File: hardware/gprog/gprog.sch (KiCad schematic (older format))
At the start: 20 parts, among them P1 ISP x2560, P2 USB, P3 ISP x48, U1 74HC126, X1 12MHz

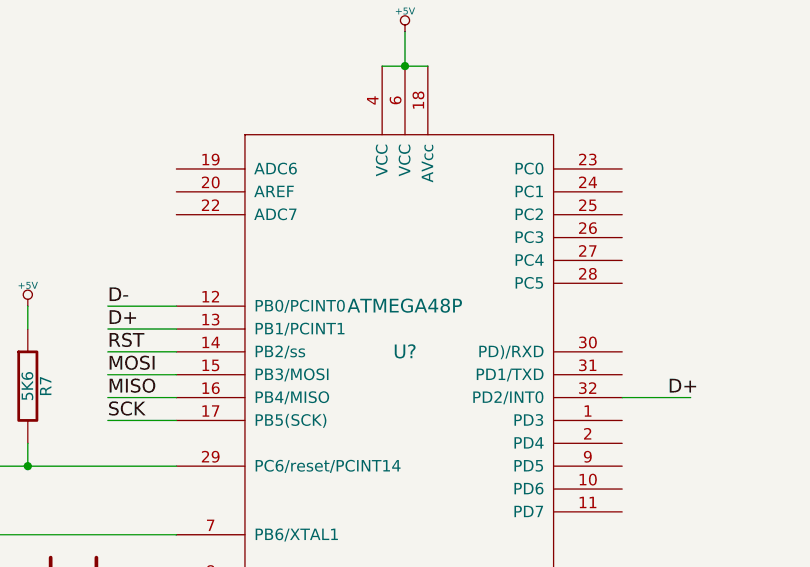
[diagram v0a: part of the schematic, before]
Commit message: Minor correction to GPRO v1.0 Schematic and component library.
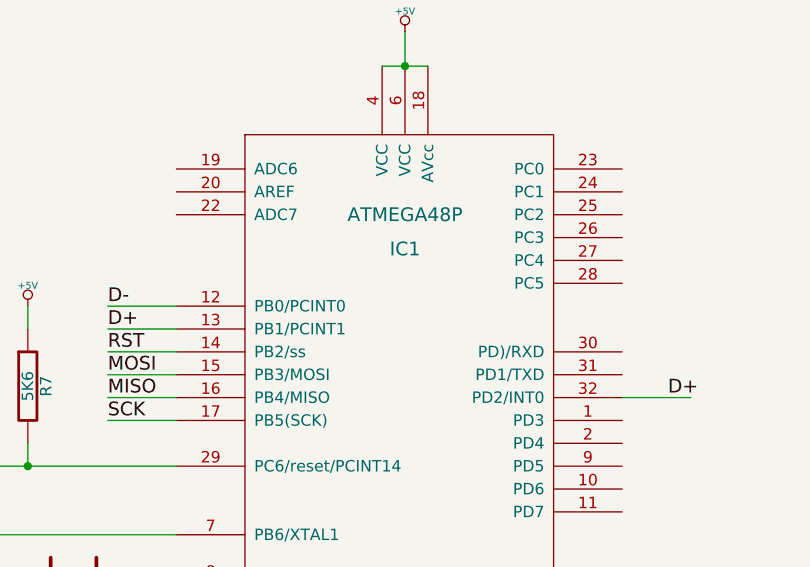
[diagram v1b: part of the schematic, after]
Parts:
- gave numbers to parts that had none: 1
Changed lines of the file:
@@
-EESchema Schematic File Version 2  date 23/11/2011 2:39:53 p.m.
+EESchema Schematic File Version 2  date 23/11/2011 3:01:04 p.m.
 LIBS:power
 LIBS:device
@@
 $EndComp
 $Comp
-L ATMEGA48P U?
+L ATMEGA48P IC1
 U 1 1 4ECC4939
 P 4200 5350
-F 0 "U?" H 4200 5350 60  0000 C CNN
-F 1 "ATMEGA48P" H 4200 5550 60  0000 C CNN
+F 0 "IC1" H 4200 5800 60  0000 C CNN
+F 1 "ATMEGA48P" H 4200 5950 60  0000 C CNN
 	1    4200 5350
 	1    0    0    -1

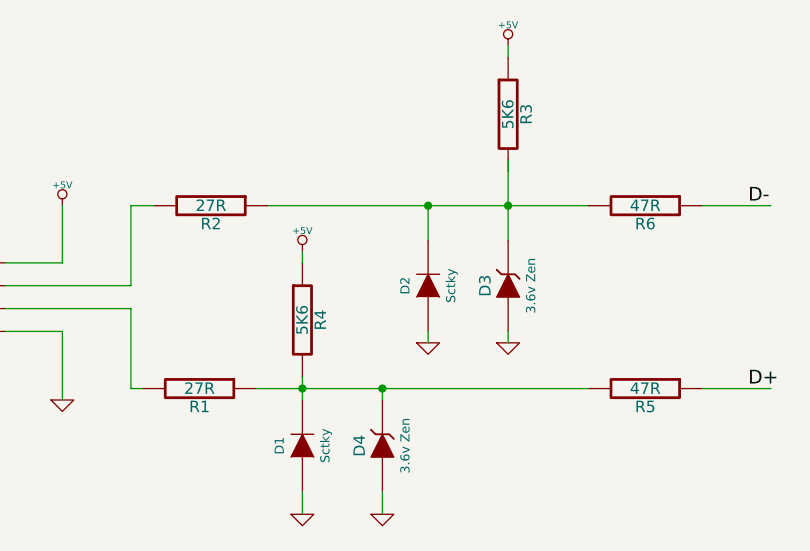
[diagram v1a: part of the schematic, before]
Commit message: As advised by JWB, corrected GPROG (USBasp) programmer circuit.
Only pull-up D- to tell USB host we are a slow speed device. Changed resistor
to 3K6 from 5K6 for better voltage matching, in theory.
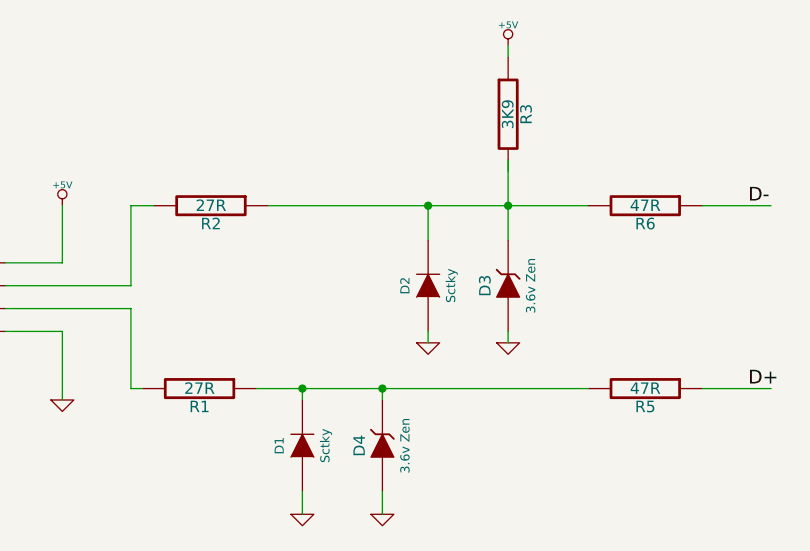
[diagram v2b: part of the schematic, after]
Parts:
- removed R4: 5K6, symbol R
- R3: value 5K6 -> 3K9
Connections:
- wire segments 93 -> 91
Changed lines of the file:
@@
-EESchema Schematic File Version 2  date 23/11/2011 3:01:04 p.m.
+EESchema Schematic File Version 2  date 24/11/2011 2:36:36 p.m.
 LIBS:power
 LIBS:device
@@
 Sheet 1 1
 Title "G9X USB Programmer"
-Date "23 nov 2011"
+Date "24 nov 2011"
 Rev "1.0"
 Comp ""
@@
 Wire Wire Line
 	4150 2400 4150 2350
-Wire Wire Line
-	3250 2050 3250 2000
 Connection ~ 3800 1800
 Wire Wire Line
@@
 Wire Wire Line
 	3250 2600 3050 2600
-Wire Wire Line
-	3250 2550 3250 2600
 Wire Wire Line
 	3250 2600 3250 2650
@@
 $EndComp
 $Comp
-L +5V #PWR?
-U 1 1 4E9129FB
-P 3250 2000
-F 0 "#PWR?" H 3250 2090 20  0001 C CNN
-F 1 "+5V" H 3250 2090 30  0000 C CNN
-	1    3250 2000
-	1    0    0    -1
-$EndComp
-$Comp
-L R R4
-U 1 1 4E9129C4
-P 3250 2300
-F 0 "R4" V 3330 2300 50  0000 C CNN
-F 1 "5K6" V 3250 2300 50  0000 C CNN
-	1    3250 2300
-	1    0    0    -1
-$EndComp
-$Comp
 L R R5
 U 1 1 4E912987
@@
 P 4150 1400
 F 0 "R3" V 4230 1400 50  0000 C CNN
-F 1 "5K6" V 4150 1400 50  0000 C CNN
+F 1 "3K9" V 4150 1400 50  0000 C CNN
 	1    4150 1400
 	1    0    0    -1

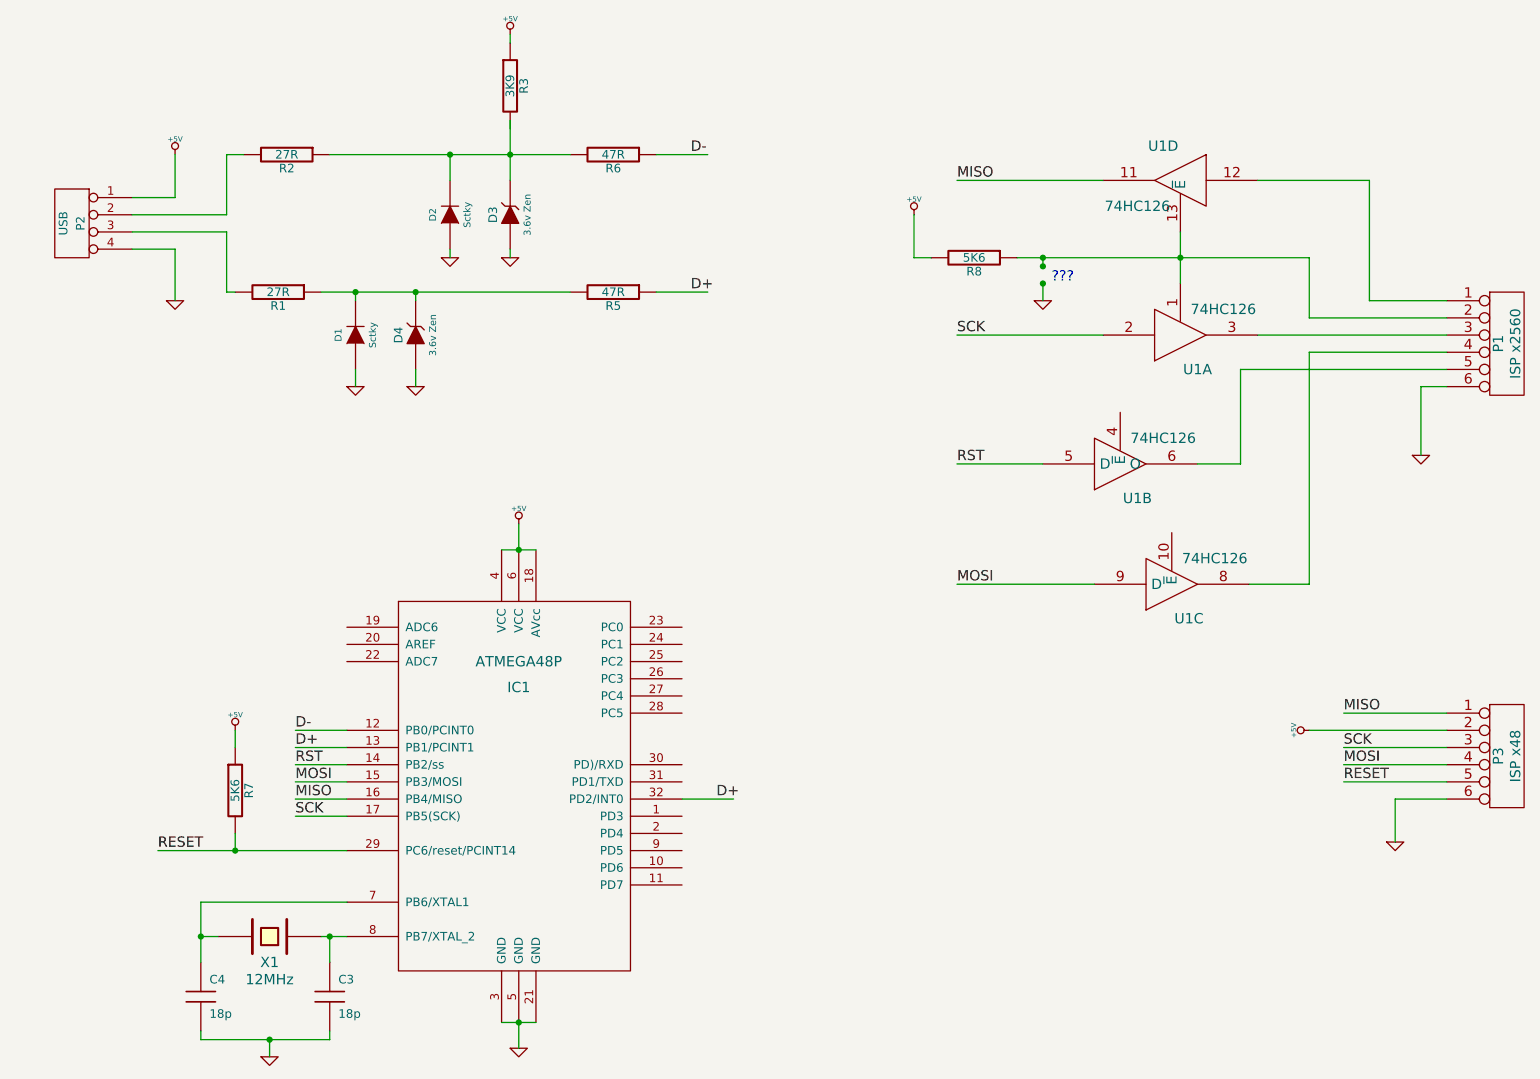
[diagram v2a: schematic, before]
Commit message: Completed draft 1 of gprog KiCAD version PCB.
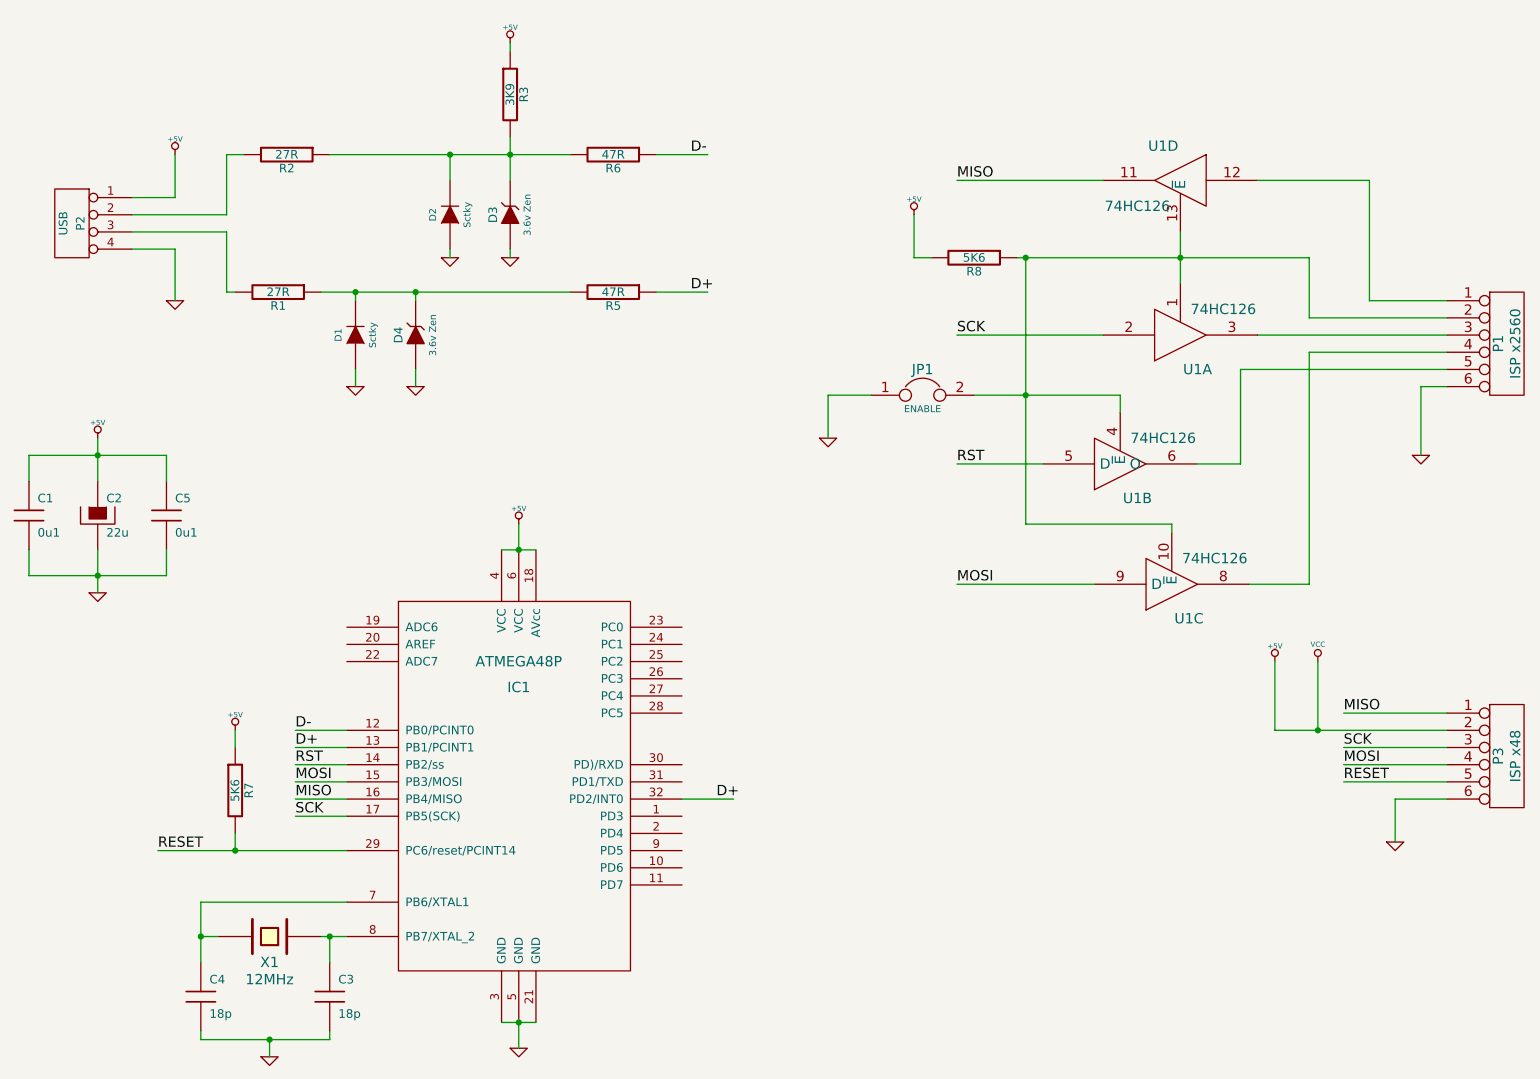
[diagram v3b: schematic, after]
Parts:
- added C1, C5: 0u1, symbol C
- added C2: 22u, symbol CAPAPOL
- added JP1: ENABLE, symbol JUMPER
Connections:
- net labels added: VCC
- wire segments 91 -> 92
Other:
- note removed: "???"
- moved on the sheet: R3
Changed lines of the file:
@@
-EESchema Schematic File Version 2  date 24/11/2011 2:36:36 p.m.
+EESchema Schematic File Version 2  date 27/11/2011 12:33:56 a.m.
 LIBS:power
 LIBS:device
@@
 Sheet 1 1
 Title "G9X USB Programmer"
-Date "24 nov 2011"
+Date "26 nov 2011"
 Rev "1.0"
 Comp ""
@@
 Comment4 ""
 $EndDescr
-Text Notes 7300 2550 0    60   ~ 0
-???
-Connection ~ 7250 2550
-Wire Wire Line
-	7250 2650 7250 2550
-Wire Wire Line
-	7100 2400 7250 2400
-Wire Wire Line
-	7250 2400 8050 2400
-Wire Wire Line
-	8050 2400 8800 2400
+Wire Wire Line
+	8600 5150 8600 4750
+Wire Wire Line
+	6850 3200 7700 3200
+Connection ~ 7150 3200
+Wire Wire Line
+	7700 3200 7700 3300
+Wire Wire Line
+	1750 3450 1750 3700
+Wire Wire Line
+	2150 3550 2150 3700
+Wire Wire Line
+	2150 3550 1350 3550
+Wire Wire Line
+	1350 3550 1350 3700
+Connection ~ 1750 4250
+Wire Wire Line
+	7100 2400 8800 2400
 Wire Wire Line
 	6600 2400 6500 2400
@@
 	6500 2400 6500 2150
 Wire Wire Line
-	2350 6900 2350 6950
-Wire Wire Line
-	2350 6950 2750 6950
-Wire Wire Line
-	2750 6950 3100 6950
+	2350 6950 2350 6900
+Wire Wire Line
+	2350 6950 3100 6950
 Wire Wire Line
 	3100 6950 3100 6900
 Connection ~ 2350 6350
 Wire Wire Line
-	2350 6500 2350 6350
-Wire Wire Line
-	2350 6350 2350 6150
+	2350 6500 2350 6150
 Wire Wire Line
 	2350 6150 3200 6150
@@
 	2550 5150 2550 5250
 Wire Wire Line
-	3200 5850 2550 5850
-Wire Wire Line
-	2550 5850 2100 5850
+	2100 5850 3200 5850
 Wire Wire Line
 	3200 5250 2900 5250
@@
 Connection ~ 4200 4100
 Wire Wire Line
-	4100 4100 4200 4100
-Wire Wire Line
-	4200 4100 4300 4100
+	4300 4100 4100 4100
 Wire Wire Line
 	9300 5800 9300 5550
@@
 	8800 4300 8450 4300
 Wire Wire Line
-	8050 2550 8050 2400
-Wire Wire Line
-	8050 2400 8050 2250
+	8050 2250 8050 2550
 Wire Wire Line
 	8800 2400 8800 2750
@@
 	2600 1800 2500 1800
 Wire Wire Line
-	3100 1800 3800 1800
-Wire Wire Line
-	3800 1800 4150 1800
-Wire Wire Line
-	4150 1800 4500 1800
-Wire Wire Line
-	4150 1100 4150 1150
+	4500 1800 3100 1800
+Wire Wire Line
+	4150 1200 4150 1150
 Wire Wire Line
 	5000 2600 5300 2600
@@
 	3800 2350 3800 2400
 Wire Wire Line
-	4500 2600 3600 2600
-Wire Wire Line
-	3600 2600 3250 2600
-Wire Wire Line
-	3250 2600 3050 2600
+	3050 2600 4500 2600
 Wire Wire Line
 	3250 2600 3250 2650
@@
 	5000 1800 5300 1800
 Wire Wire Line
-	4150 1600 4150 1800
-Wire Wire Line
-	4150 1800 4150 1950
+	4150 1950 4150 1700
 Wire Wire Line
 	2550 2600 2500 2600
@@
 	7600 1950 6750 1950
 Wire Wire Line
-	9600 5150 8800 5150
+	9600 5150 8600 5150
 Wire Wire Line
 	9600 5350 9000 5350
@@
 	4200 3950 4200 4100
 Wire Wire Line
-	4100 6850 4200 6850
-Wire Wire Line
-	4200 6850 4300 6850
+	4300 6850 4100 6850
 Connection ~ 4200 6850
 Wire Wire Line
@@
 Connection ~ 2550 5850
 Wire Wire Line
-	3050 6350 3100 6350
-Wire Wire Line
-	3100 6350 3200 6350
-Wire Wire Line
-	2350 6350 2450 6350
+	3200 6350 3050 6350
+Wire Wire Line
+	2450 6350 2350 6350
 Wire Wire Line
 	3100 6500 3100 6350
@@
 Connection ~ 2750 6950
 Wire Wire Line
-	7250 2400 7250 2450
-Connection ~ 7250 2400
-Connection ~ 7250 2450
-$Comp
-L GND #PWR?
-U 1 1 4ECC4DFB
-P 7250 2650
-F 0 "#PWR?" H 7250 2650 30  0001 C CNN
-F 1 "GND" H 7250 2580 30  0001 C CNN
-	1    7250 2650
+	2150 4250 2150 4100
+Wire Wire Line
+	2150 4250 1350 4250
+Wire Wire Line
+	1350 4250 1350 4100
+Wire Wire Line
+	1750 4350 1750 4100
+Connection ~ 1750 3550
+Wire Wire Line
+	8000 4000 8000 3950
+Wire Wire Line
+	7150 3950 8000 3950
+Wire Wire Line
+	7150 2400 7150 3950
+Connection ~ 7150 2400
+Wire Wire Line
+	6000 3450 6000 3200
+Wire Wire Line
+	6000 3200 6250 3200
+Wire Wire Line
+	8850 4750 8850 5150
+Connection ~ 8850 5150
+$Comp
+L VCC #PWR01
+U 1 1 4ED0B44E
+P 8850 4750
+F 0 "#PWR01" H 8850 4850 30  0001 C CNN
+F 1 "VCC" H 8850 4850 30  0000 C CNN
+	1    8850 4750
+	1    0    0    -1
+$EndComp
+$Comp
+L GND #PWR02
+U 1 1 4ED0AC2D
+P 6000 3450
+F 0 "#PWR02" H 6000 3450 30  0001 C CNN
+F 1 "GND" H 6000 3380 30  0001 C CNN
+	1    6000 3450
+	1    0    0    -1
+$EndComp
+$Comp
+L JUMPER JP1
+U 1 1 4ED0AC1E
+P 6550 3200
+F 0 "JP1" H 6550 3350 60  0000 C CNN
+F 1 "ENABLE" H 6550 3120 40  0000 C CNN
+	1    6550 3200
+	1    0    0    -1
+$EndComp
+$Comp
+L +5V #PWR03
+U 1 1 4ED08824
+P 1750 3450
+F 0 "#PWR03" H 1750 3540 20  0001 C CNN
+F 1 "+5V" H 1750 3540 30  0000 C CNN
+	1    1750 3450
+	1    0    0    -1
+$EndComp
+$Comp
+L GND #PWR04
+U 1 1 4ED08810
+P 1750 4350
+F 0 "#PWR04" H 1750 4350 30  0001 C CNN
+F 1 "GND" H 1750 4280 30  0001 C CNN
+	1    1750 4350
+	1    0    0    -1
+$EndComp
+$Comp
+L CAPAPOL C2
+U 1 1 4ED087CB
+P 1750 3900
+F 0 "C2" H 1800 4000 50  0000 L CNN
+F 1 "22u" H 1800 3800 50  0000 L CNN
+	1    1750 3900
+	1    0    0    -1
+$EndComp
+$Comp
+L C C5
+U 1 1 4ED087AC
+P 2150 3900
+F 0 "C5" H 2200 4000 50  0000 L CNN
+F 1 "0u1" H 2200 3800 50  0000 L CNN
+	1    2150 3900
+	1    0    0    -1
+$EndComp
+$Comp
+L C C1
+U 1 1 4ED087A6
+P 1350 3900
+F 0 "C1" H 1400 4000 50  0000 L CNN
+F 1 "0u1" H 1400 3800 50  0000 L CNN
+	1    1350 3900
 	1    0    0    -1
 $EndComp
@@
 D+
 $Comp
-L GND #PWR?
+L GND #PWR05
 U 1 1 4ECC4B90
 P 2750 7050
-F 0 "#PWR?" H 2750 7050 30  0001 C CNN
+F 0 "#PWR05" H 2750 7050 30  0001 C CNN
 F 1 "GND" H 2750 6980 30  0001 C CNN
 	1    2750 7050
@@
 $EndComp
 $Comp
-L +5V #PWR?
+L +5V #PWR06
 U 1 1 4ECC4A1D
 P 2550 5150
-F 0 "#PWR?" H 2550 5240 20  0001 C CNN
+F 0 "#PWR06" H 2550 5240 20  0001 C CNN
 F 1 "+5V" H 2550 5240 30  0000 C CNN
 	1    2550 5150
@@
 D-
 $Comp
-L GND #PWR?
+L GND #PWR07
 U 1 1 4ECC4963
 P 4200 7000
-F 0 "#PWR?" H 4200 7000 30  0001 C CNN
+F 0 "#PWR07" H 4200 7000 30  0001 C CNN
 F 1 "GND" H 4200 6930 30  0001 C CNN
 	1    4200 7000
@@
 $EndComp
 $Comp
-L +5V #PWR?
+L +5V #PWR08
 U 1 1 4ECC494B
 P 4200 3950
-F 0 "#PWR?" H 4200 4040 20  0001 C CNN
+F 0 "#PWR08" H 4200 4040 20  0001 C CNN
 F 1 "+5V" H 4200 4040 30  0000 C CNN
 	1    4200 3950
@@
 MISO
 $Comp
-L +5V #PWR?
+L +5V #VCC09
 U 1 1 4ECB2F25
-P 8800 5150
-F 0 "#PWR?" H 8800 5240 20  0001 C CNN
-F 1 "+5V" H 8800 5240 30  0000 C CNN
-	1    8800 5150
-	0    -1   -1   0
-$EndComp
-$Comp
-L GND #PWR?
+P 8600 4750
+F 0 "#VCC09" H 8600 4840 20  0001 C CNN
+F 1 "+5V" H 8600 4840 30  0000 C CNN
+	1    8600 4750
+	1    0    0    -1
+$EndComp
+$Comp
+L GND #PWR010
 U 1 1 4ECB2F15
 P 9300 5800
-F 0 "#PWR?" H 9300 5800 30  0001 C CNN
+F 0 "#PWR010" H 9300 5800 30  0001 C CNN
 F 1 "GND" H 9300 5730 30  0001 C CNN
 	1    9300 5800
@@
 MISO
 $Comp
-L GND #PWR?
+L GND #PWR011
 U 1 1 4ECB2CC4
 P 9450 3550
-F 0 "#PWR?" H 9450 3550 30  0001 C CNN
+F 0 "#PWR011" H 9450 3550 30  0001 C CNN
 F 1 "GND" H 9450 3480 30  0001 C CNN
 	1    9450 3550
@@
 $EndComp
 $Comp
-L +5V #PWR?
+L +5V #PWR012
 U 1 1 4ECB2C7C
 P 6500 2150
-F 0 "#PWR?" H 6500 2240 20  0001 C CNN
+F 0 "#PWR012" H 6500 2240 20  0001 C CNN
 F 1 "+5V" H 6500 2240 30  0000 C CNN
 	1    6500 2150
@@
 D-
 $Comp
-L +5V #PWR?
+L +5V #PWR013
 U 1 1 4E912AAE
-P 4150 1100
-F 0 "#PWR?" H 4150 1190 20  0001 C CNN
-F 1 "+5V" H 4150 1190 30  0000 C CNN
-	1    4150 1100
+P 4150 1150
+F 0 "#PWR013" H 4150 1240 20  0001 C CNN
+F 1 "+5V" H 4150 1240 30  0000 C CNN
+	1    4150 1150
 	1    0    0    -1
 $EndComp
@@
 $EndComp
 $Comp
-L GND #PWR?
+L GND #PWR014
 U 1 1 4E912A17
 P 4150 2400
-F 0 "#PWR?" H 4150 2400 30  0001 C CNN
+F 0 "#PWR014" H 4150 2400 30  0001 C CNN
 F 1 "GND" H 4150 2330 30  0001 C CNN
 	1    4150 2400
@@
 $EndComp
 $Comp
-L GND #PWR?
+L GND #PWR015
 U 1 1 4E912A11
 P 3800 2400
-F 0 "#PWR?" H 3800 2400 30  0001 C CNN
+F 0 "#PWR015" H 3800 2400 30  0001 C CNN
 F 1 "GND" H 3800 2330 30  0001 C CNN
 	1    3800 2400
@@
 $EndComp
 $Comp
-L GND #PWR?
+L GND #PWR016
 U 1 1 4E912A0A
 P 3600 3150
-F 0 "#PWR?" H 3600 3150 30  0001 C CNN
+F 0 "#PWR016" H 3600 3150 30  0001 C CNN
 F 1 "GND" H 3600 3080 30  0001 C CNN
 	1    3600 3150
@@
 $EndComp
 $Comp
-L GND #PWR?
+L GND #PWR017
 U 1 1 4E912A03
 P 3250 3150
-F 0 "#PWR?" H 3250 3150 30  0001 C CNN
+F 0 "#PWR017" H 3250 3150 30  0001 C CNN
 F 1 "GND" H 3250 3080 30  0001 C CNN
 	1    3250 3150
@@
 L R R3
 U 1 1 4E91296B
-P 4150 1400
-F 0 "R3" V 4230 1400 50  0000 C CNN
-F 1 "3K9" V 4150 1400 50  0000 C CNN
-	1    4150 1400
+P 4150 1450
+F 0 "R3" V 4230 1450 50  0000 C CNN
+F 1 "3K9" V 4150 1450 50  0000 C CNN
+	1    4150 1450
 	1    0    0    -1
 $EndComp
@@
 $EndComp
 $Comp
-L GND #PWR?
+L GND #PWR018
 U 1 1 4E91292A
 P 2200 2650
-F 0 "#PWR?" H 2200 2650 30  0001 C CNN
+F 0 "#PWR018" H 2200 2650 30  0001 C CNN
 F 1 "GND" H 2200 2580 30  0001 C CNN
 	1    2200 2650
@@
 $EndComp
 $Comp
-L +5V #PWR?
+L +5V #PWR019
 U 1 1 4E91291D
 P 2200 1800
-F 0 "#PWR?" H 2200 1890 20  0001 C CNN
+F 0 "#PWR019" H 2200 1890 20  0001 C CNN
 F 1 "+5V" H 2200 1890 30  0000 C CNN
 	1    2200 1800
